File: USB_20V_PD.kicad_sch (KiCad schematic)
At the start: 25 parts, among them J1 Screw_Terminal_01x02, J2 USB_C_Receptacle, Q1 SI3421DV, Q2 SI3421DV, U1 CYPD3177_24x

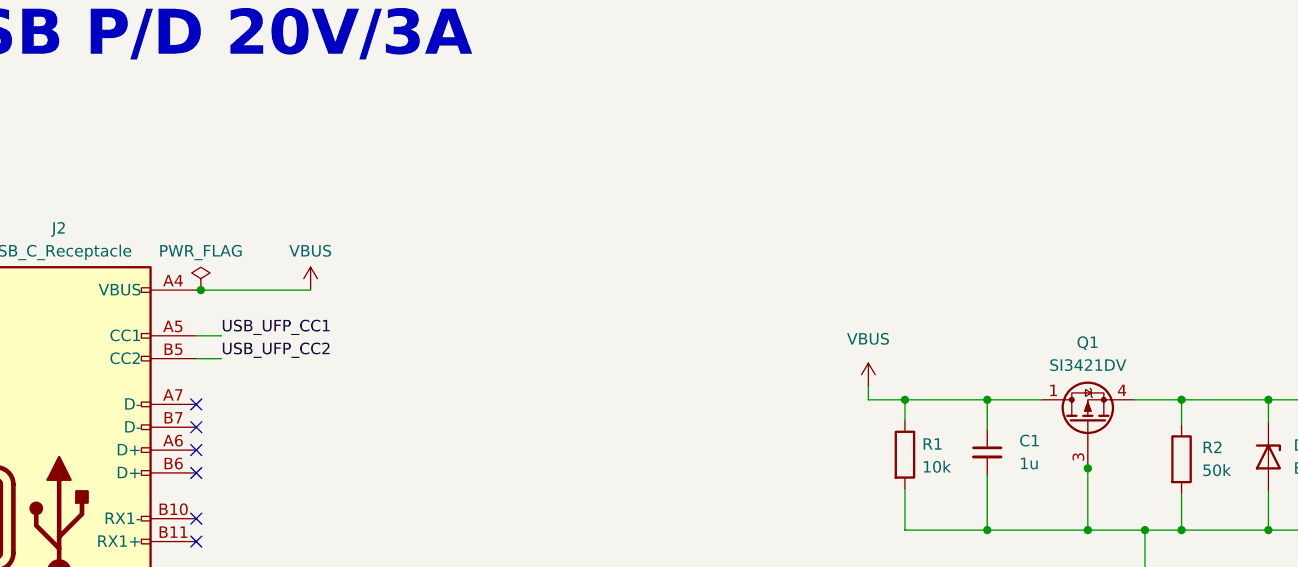
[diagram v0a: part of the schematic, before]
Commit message: update readme and schematics
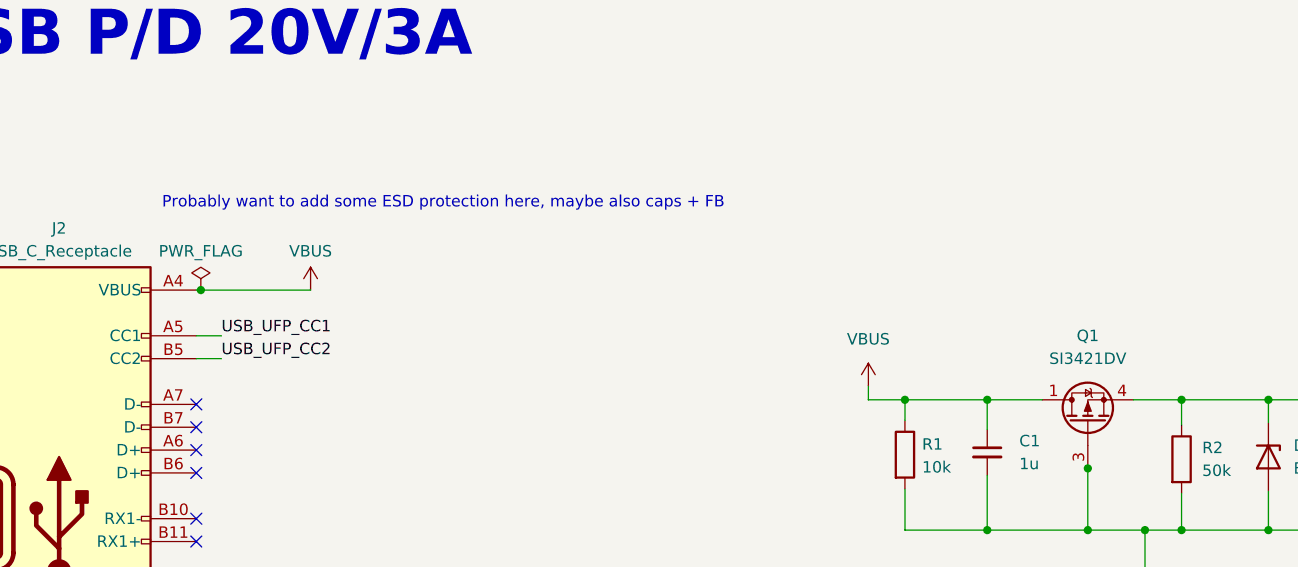
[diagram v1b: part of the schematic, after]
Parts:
- Q1, Q2: symbol catSink:SI3421DV -> CakeUSB:SI3421DV
- U1: symbol Cake_USB:CYPD3177_24x -> CakeUSB:CYPD3177_24x
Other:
- note added: "Probably want to add some ESD protection here, maybe also caps + FB"
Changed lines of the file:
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@@
+    (effects (font (size 1.27 1.27)) (justify left bottom))
+  )
+  (text "Probably want to add some ESD protection here, maybe also caps + FB"
+    (at 41.91 39.37 0)
     (effects (font (size 1.27 1.27)) (justify left bottom))
   )
@@
     )
   )
-  (symbol (lib_id "catSink:SI3421DV") (at 144.78 60.452 0) (unit 1)
-    (in_bom yes) (on_board yes) (dnp no) (fields_autoplaced)
-    (property "Reference" "Q1" (at 144.78 54.102 0)
-      (effects (font (size 1.27 1.27)))
-    )
-    (property "Value" "SI3421DV" (at 144.78 56.642 0)
-      (effects (font (size 1.27 1.27)))
-    )
-    (property "Footprint" "Package_TO_SOT_SMD:SOT-23-6" (at 170.18 60.452 0)
-      (effects (font (size 1.27 1.27)) hide)
-    )
-    (property "Datasheet" "https://www.mouser.mx/datasheet/2/427/si3421dv-1764435.pdf" (at 144.78 62.992 90)
-      (effects (font (size 1.27 1.27)) hide)
-    )
-    (property "manf#" "SI3421DV-T1-GE3" (at 162.56 57.912 0)
+  (symbol (lib_id "CakeUSB:SI3421DV") (at 144.78 60.452 0) (unit 1)
+    (in_bom yes) (on_board yes) (dnp no) (fields_autoplaced)
+    (property "Reference" "Q1" (at 144.78 53.34 0)
+      (effects (font (size 1.27 1.27)))
+    )
+    (property "Value" "SI3421DV" (at 144.78 55.88 0)
+      (effects (font (size 1.27 1.27)))
+    )
+    (property "Footprint" "Package_TO_SOT_SMD:SOT-23-6" (at 168.91 50.292 0)
+      (effects (font (size 1.27 1.27)) hide)
+    )
+    (property "Datasheet" "https://www.mouser.mx/datasheet/2/427/si3421dv-1764435.pdf" (at 185.42 52.832 0)
+      (effects (font (size 1.27 1.27)) hide)
+    )
+    (property "manf#" "SI3421DV-T1-GE3" (at 161.29 47.752 0)
       (effects (font (size 1.27 1.27)) hide)
     )
@@
     )
   )
-  (symbol (lib_id "Cake_USB:CYPD3177_24x") (at 157.48 106.68 0) (unit 1)
+  (symbol (lib_id "CakeUSB:CYPD3177_24x") (at 157.48 106.68 0) (unit 1)
     (in_bom yes) (on_board yes) (dnp no)
     (property "Reference" "U1" (at 172.72 92.71 0)
@@
     )
   )
-  (symbol (lib_id "catSink:SI3421DV") (at 178.054 60.452 0) (mirror y) (unit 1)
+  (symbol (lib_id "CakeUSB:SI3421DV") (at 178.054 60.452 0) (mirror y) (unit 1)
     (in_bom yes) (on_board yes) (dnp no)
     (property "Reference" "Q2" (at 178.054 54.102 0)
@@
       (effects (font (size 1.27 1.27)))
     )
-    (property "Footprint" "Package_TO_SOT_SMD:SOT-23-6" (at 152.654 60.452 0)
-      (effects (font (size 1.27 1.27)) hide)
-    )
-    (property "Datasheet" "https://www.mouser.mx/datasheet/2/427/si3421dv-1764435.pdf" (at 178.054 62.992 90)
-      (effects (font (size 1.27 1.27)) hide)
-    )
-    (property "manf#" "SI3421DV-T1-GE3" (at 160.274 57.912 0)
-      (effects (font (size 1.27 1.27)) hide)
-    )
+    (property "Footprint" "Package_TO_SOT_SMD:SOT-23-6" (at 153.924 50.292 0)
+      (effects (font (size 1.27 1.27)) hide)
+    )
+    (property "Datasheet" "https://www.mouser.mx/datasheet/2/427/si3421dv-1764435.pdf" (at 137.414 52.832 0)
+      (effects (font (size 1.27 1.27)) hide)
+    )
+    (property "manf#" "SI3421DV-T1-GE3" (at 161.544 47.752 0)
+      (effects (font (size 1.27 1.27)) hide)
+    )
